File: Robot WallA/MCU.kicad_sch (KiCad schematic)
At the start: 0 parts

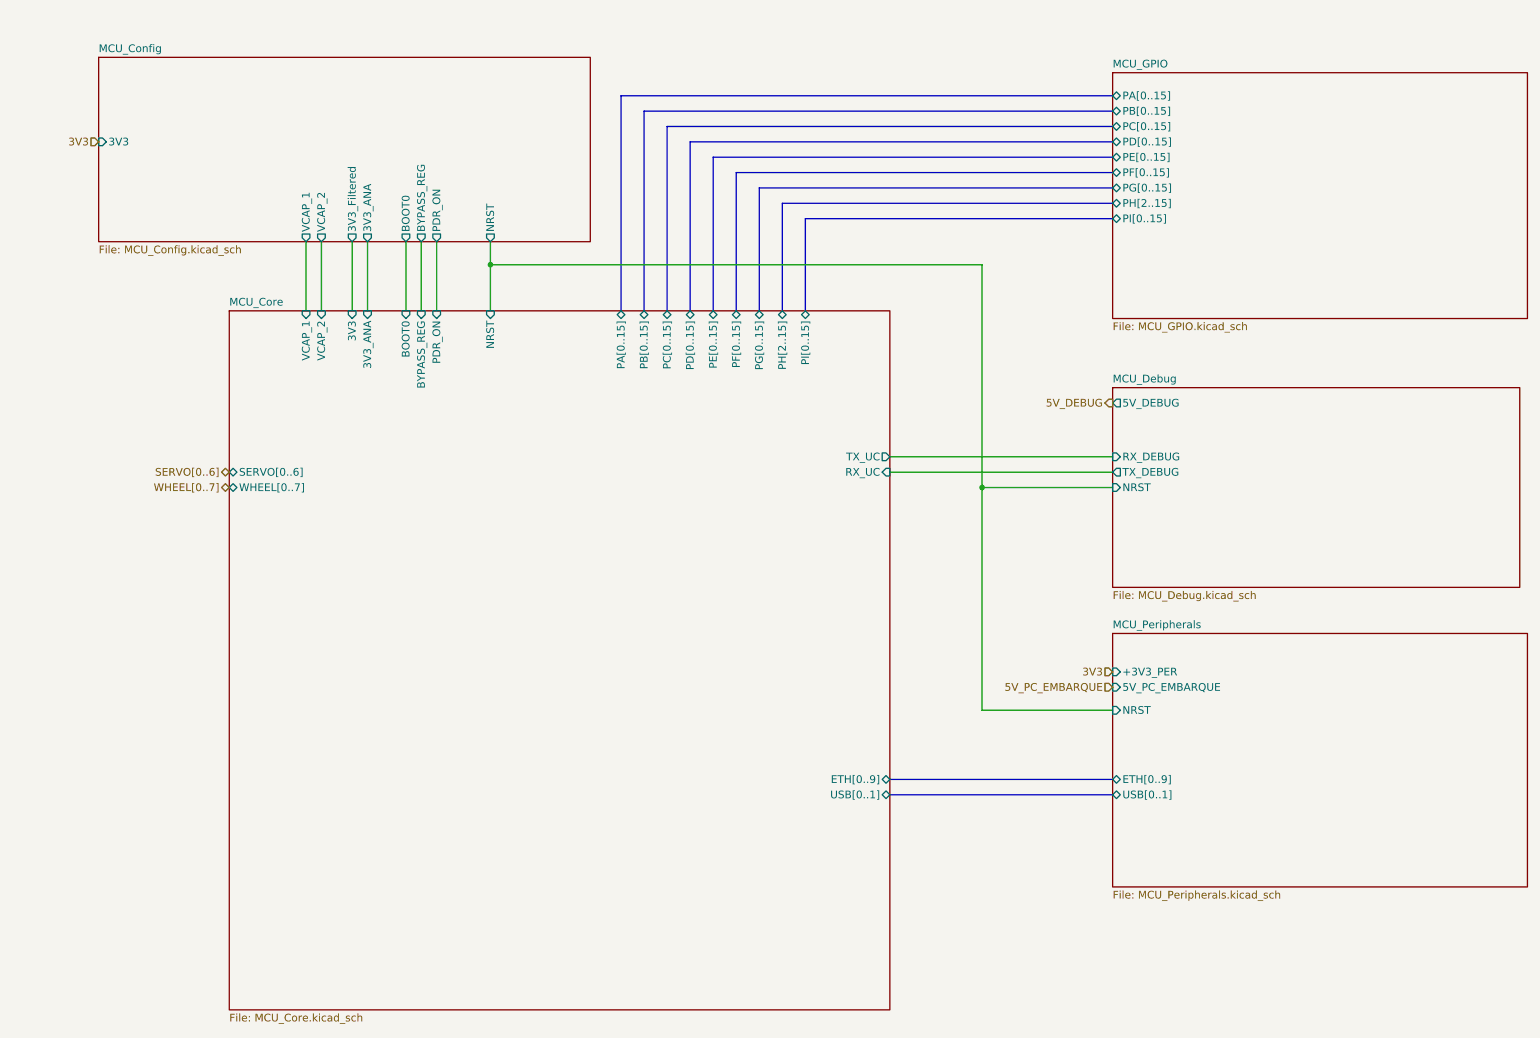
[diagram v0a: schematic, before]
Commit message: Continued to link MCU pins, Added a sheet for servomotors and optional 2 DC motors.
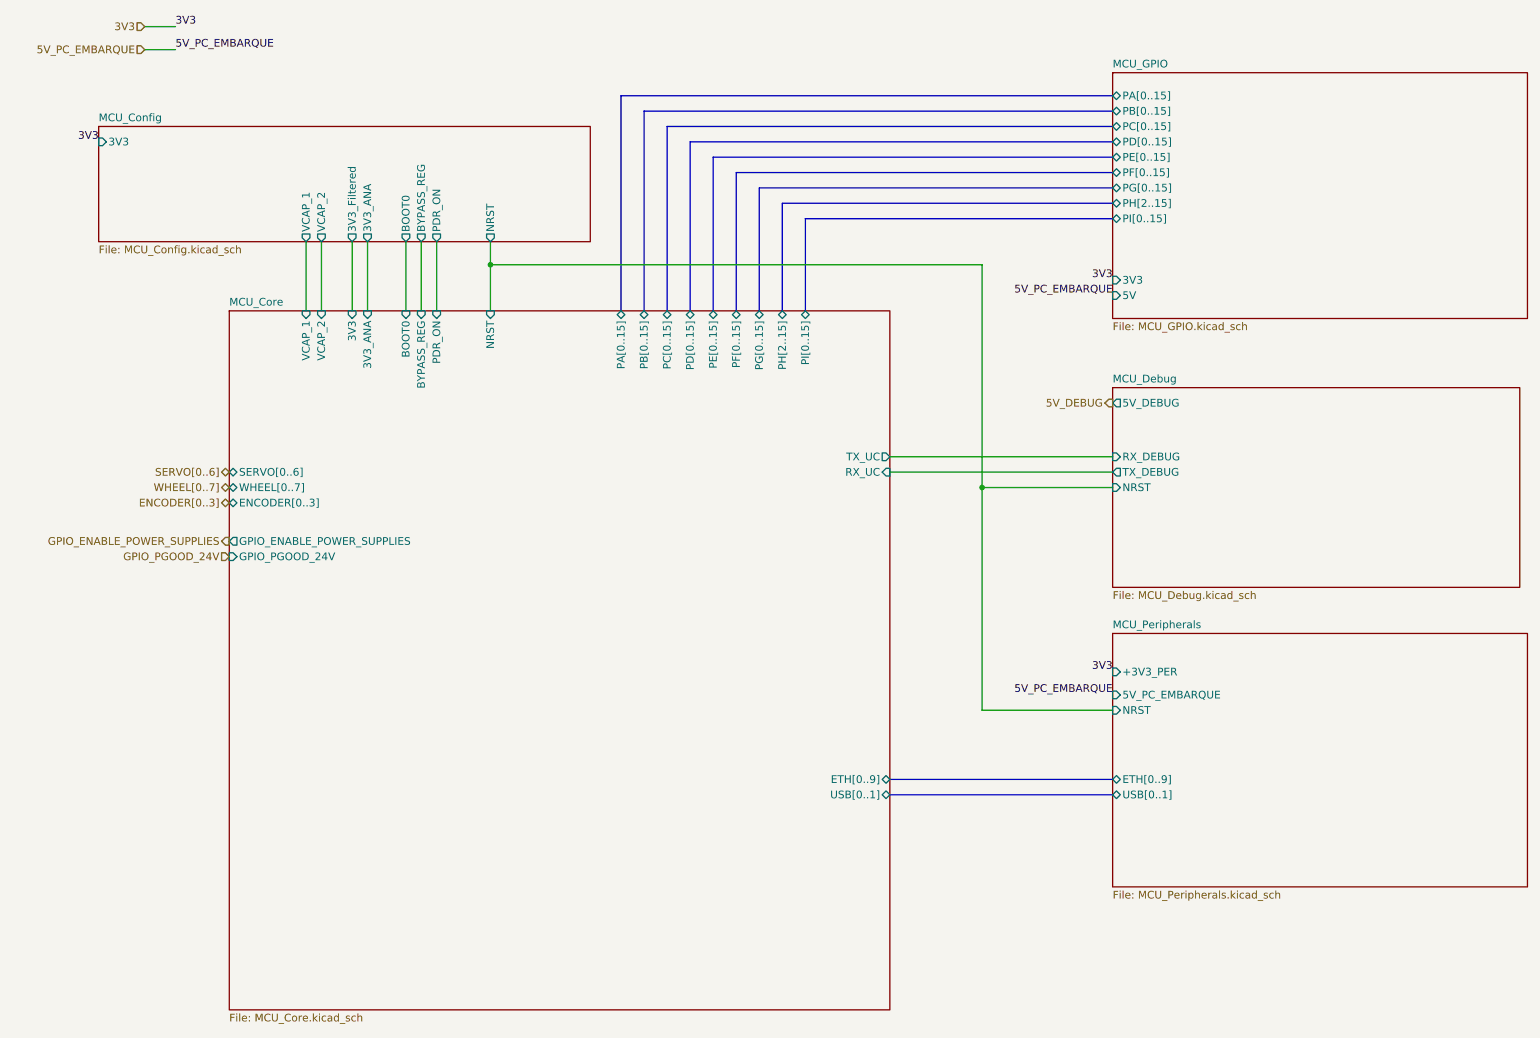
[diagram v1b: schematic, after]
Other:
- sheet MCU_Core ports: added ENCODER[0..3], GPIO_ENABLE_POWER_SUPPLIES, GPIO_PGOOD_24V; removed none
- sheet MCU_GPIO ports: added 3V3, 5V; removed none
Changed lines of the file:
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@@
+		)
+	)
+	(wire
+		(pts
+			(xy 39.37 21.59) (xy 34.29 21.59)
+		)
+		(stroke
+			(width 0)
+			(type default)
+		)
+	)
+	(wire
+		(pts
+			(xy 39.37 17.78) (xy 34.29 17.78)
+		)
+		(stroke
+			(width 0)
+			(type default)
 		)
 	)
@@
 			(width 0)
 			(type default)
+		)
+	)
+	(label "5V_PC_EMBARQUE"
+		(at 194.31 128.27 180)
+		(effects
+			(font
+				(size 1.27 1.27)
+			)
+			(justify right bottom)
+		)
+	)
+	(label "5V_PC_EMBARQUE"
+		(at 39.37 21.59 0)
+		(effects
+			(font
+				(size 1.27 1.27)
+			)
+			(justify left bottom)
+		)
+	)
+	(label "3V3"
+		(at 26.67 36.83 180)
+		(effects
+			(font
+				(size 1.27 1.27)
+			)
+			(justify right bottom)
+		)
+	)
+	(label "3V3"
+		(at 194.31 59.69 180)
+		(effects
+			(font
+				(size 1.27 1.27)
+			)
+			(justify right bottom)
+		)
+	)
+	(label "3V3"
+		(at 39.37 17.78 0)
+		(effects
+			(font
+				(size 1.27 1.27)
+			)
+			(justify left bottom)
+		)
+	)
+	(label "3V3"
+		(at 194.31 124.46 180)
+		(effects
+			(font
+				(size 1.27 1.27)
+			)
+			(justify right bottom)
+		)
+	)
+	(label "5V_PC_EMBARQUE"
+		(at 194.31 62.23 180)
+		(effects
+			(font
+				(size 1.27 1.27)
+			)
+			(justify right bottom)
+		)
+	)
+	(hierarchical_label "GPIO_PGOOD_24V"
+		(shape input)
+		(at 48.26 105.41 180)
+		(effects
+			(font
+				(size 1.27 1.27)
+			)
+			(justify right)
 		)
 	)
@@
 		)
 	)
-	(hierarchical_label "5V_PC_EMBARQUE"
-		(shape input)
-		(at 194.31 127 180)
-		(effects
-			(font
-				(size 1.27 1.27)
-			)
-			(justify right)
-		)
-	)
-	(hierarchical_label "3V3"
-		(shape input)
-		(at 26.67 36.83 180)
-		(effects
-			(font
-				(size 1.27 1.27)
-			)
-			(justify right)
-		)
-	)
 	(hierarchical_label "SERVO[0..6]"
 		(shape bidirectional)
@@
 		)
 	)
+	(hierarchical_label "ENCODER[0..3]"
+		(shape bidirectional)
+		(at 48.26 96.52 180)
+		(effects
+			(font
+				(size 1.27 1.27)
+			)
+			(justify right)
+		)
+	)
+	(hierarchical_label "5V_PC_EMBARQUE"
+		(shape input)
+		(at 34.29 21.59 180)
+		(effects
+			(font
+				(size 1.27 1.27)
+			)
+			(justify right)
+		)
+	)
+	(hierarchical_label "GPIO_ENABLE_POWER_SUPPLIES"
+		(shape output)
+		(at 48.26 102.87 180)
+		(effects
+			(font
+				(size 1.27 1.27)
+			)
+			(justify right)
+		)
+	)
 	(hierarchical_label "3V3"
 		(shape input)
-		(at 194.31 124.46 180)
+		(at 34.29 17.78 180)
 		(effects
 			(font
@@
 		)
 		(instances
-			(project "PCB"
+			(project "Robot WallA"
 				(path "/117fd49e-499d-4b54-b58c-f6b538ecca4a/b9176f6a-4299-4bca-a59b-5ff3df09c616"
 					(page "6")
@@
 		)
 		(pin "5V_PC_EMBARQUE" input
-			(at 194.31 127 180)
+			(at 194.31 128.27 180)
 			(effects
 				(font
@@
 		)
 		(instances
-			(project "PCB"
+			(project "Robot WallA"
 				(path "/117fd49e-499d-4b54-b58c-f6b538ecca4a/b9176f6a-4299-4bca-a59b-5ff3df09c616"
 					(page "8")
@@
 	)
 	(sheet
-		(at 26.67 22.86)
-		(size 81.28 30.48)
+		(at 26.67 34.29)
+		(size 81.28 19.05)
 		(exclude_from_sim no)
 		(in_bom yes)
@@
 		)
 		(property "Sheetname" "MCU_Config"
-			(at 26.67 22.1484 0)
+			(at 26.67 33.5784 0)
 			(effects
 				(font
@@
 		)
 		(instances
-			(project "PCB"
+			(project "Robot WallA"
 				(path "/117fd49e-499d-4b54-b58c-f6b538ecca4a/b9176f6a-4299-4bca-a59b-5ff3df09c616"
 					(page "9")
@@
 			)
 		)
+		(pin "ENCODER[0..3]" bidirectional
+			(at 48.26 96.52 180)
+			(effects
+				(font
+					(size 1.27 1.27)
+				)
+				(justify left)
+			)
+		)
+		(pin "GPIO_ENABLE_POWER_SUPPLIES" output
+			(at 48.26 102.87 180)
+			(effects
+				(font
+					(size 1.27 1.27)
+				)
+				(justify left)
+			)
+		)
+		(pin "GPIO_PGOOD_24V" input
+			(at 48.26 105.41 180)
+			(effects
+				(font
+					(size 1.27 1.27)
+				)
+				(justify left)
+			)
+		)
 		(instances
-			(project "PCB"
+			(project "Robot WallA"
 				(path "/117fd49e-499d-4b54-b58c-f6b538ecca4a/b9176f6a-4299-4bca-a59b-5ff3df09c616"
 					(page "10")
@@
 			)
 		)
+		(pin "3V3" input
+			(at 194.31 59.69 180)
+			(effects
+				(font
+					(size 1.27 1.27)
+				)
+				(justify left)
+			)
+		)
+		(pin "5V" input
+			(at 194.31 62.23 180)
+			(effects
+				(font
+					(size 1.27 1.27)
+				)
+				(justify left)
+			)
+		)
 		(instances
-			(project "PCB"
+			(project "Robot WallA"
 				(path "/117fd49e-499d-4b54-b58c-f6b538ecca4a/b9176f6a-4299-4bca-a59b-5ff3df09c616"
 					(page "7")

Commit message: Defined every footprints
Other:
- sheet MCU_Core ports: added SECONDARY_MOTOR[0..7]; removed none
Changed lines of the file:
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@@
+		)
+	)
+	(hierarchical_label "SECONDARY_MOTOR[0..7]"
+		(shape bidirectional)
+		(at 48.26 91.44 180)
+		(effects
+			(font
+				(size 1.27 1.27)
+			)
+			(justify right)
 		)
 	)
@@
 	(hierarchical_label "WHEEL[0..7]"
 		(shape bidirectional)
-		(at 48.26 93.98 180)
+		(at 48.26 86.36 180)
 		(effects
 			(font
@@
 	(hierarchical_label "SERVO[0..6]"
 		(shape bidirectional)
-		(at 48.26 91.44 180)
+		(at 48.26 83.82 180)
 		(effects
 			(font
@@
 	(hierarchical_label "ENCODER[0..3]"
 		(shape bidirectional)
-		(at 48.26 96.52 180)
+		(at 48.26 88.9 180)
 		(effects
 			(font
@@
 			(project "Robot WallA"
 				(path "/117fd49e-499d-4b54-b58c-f6b538ecca4a/b9176f6a-4299-4bca-a59b-5ff3df09c616"
-					(page "8")
+					(page "5")
 				)
 			)
@@
 			(project "Robot WallA"
 				(path "/117fd49e-499d-4b54-b58c-f6b538ecca4a/b9176f6a-4299-4bca-a59b-5ff3df09c616"
-					(page "9")
+					(page "4")
 				)
 			)
@@
 		)
 		(pin "SERVO[0..6]" bidirectional
-			(at 48.26 91.44 180)
+			(at 48.26 83.82 180)
 			(effects
 				(font
@@
 		)
 		(pin "WHEEL[0..7]" bidirectional
-			(at 48.26 93.98 180)
+			(at 48.26 86.36 180)
 			(effects
 				(font
@@
 		)
 		(pin "ENCODER[0..3]" bidirectional
-			(at 48.26 96.52 180)
+			(at 48.26 88.9 180)
 			(effects
 				(font
@@
 		(pin "GPIO_PGOOD_24V" input
 			(at 48.26 105.41 180)
+			(effects
+				(font
+					(size 1.27 1.27)
+				)
+				(justify left)
+			)
+		)
+		(pin "SECONDARY_MOTOR[0..7]" bidirectional
+			(at 48.26 91.44 180)
 			(effects
 				(font
@@
 			(project "Robot WallA"
 				(path "/117fd49e-499d-4b54-b58c-f6b538ecca4a/b9176f6a-4299-4bca-a59b-5ff3df09c616"
-					(page "10")
-				)
-			)
+					(page "3")
+				)
+			)

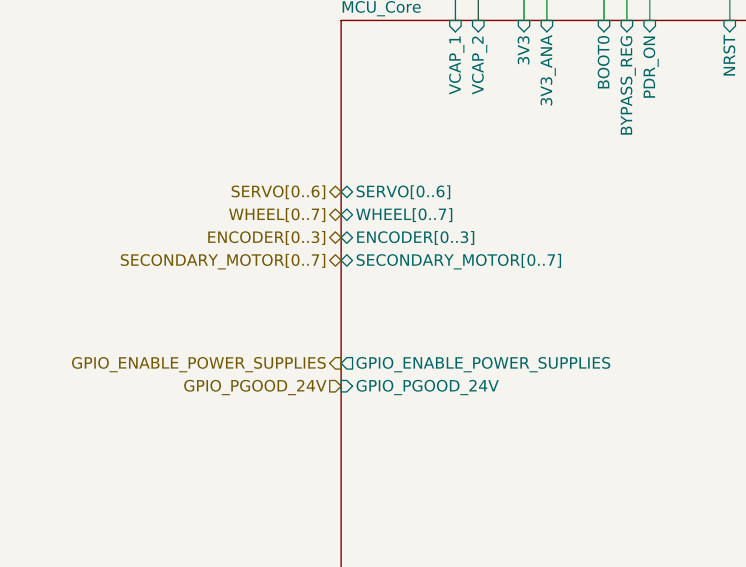
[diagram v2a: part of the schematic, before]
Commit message: Updated USB UART converter, Linked telemeter sensors.
Updated components indicators
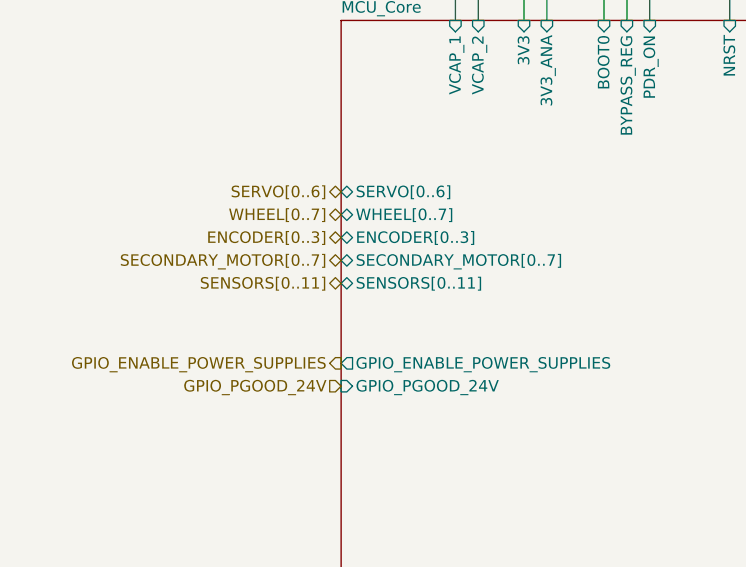
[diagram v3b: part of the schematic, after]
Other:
- sheet MCU_Core ports: added SENSORS[0..11]; removed none
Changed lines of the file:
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@@
+		)
+	)
+	(hierarchical_label "SENSORS[0..11]"
+		(shape bidirectional)
+		(at 48.26 93.98 180)
+		(effects
+			(font
+				(size 1.27 1.27)
+			)
+			(justify right)
 		)
 	)
@@
 			(effects
 				(font
+					(size 1.27 1.27)
+				)
+				(justify left)
+			)
+		)
+		(pin "SENSORS[0..11]" bidirectional
+			(at 48.26 93.98 180)
+			(effects
+				(font

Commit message: Added standard switchs, debug leds and 12V and 5V connectors
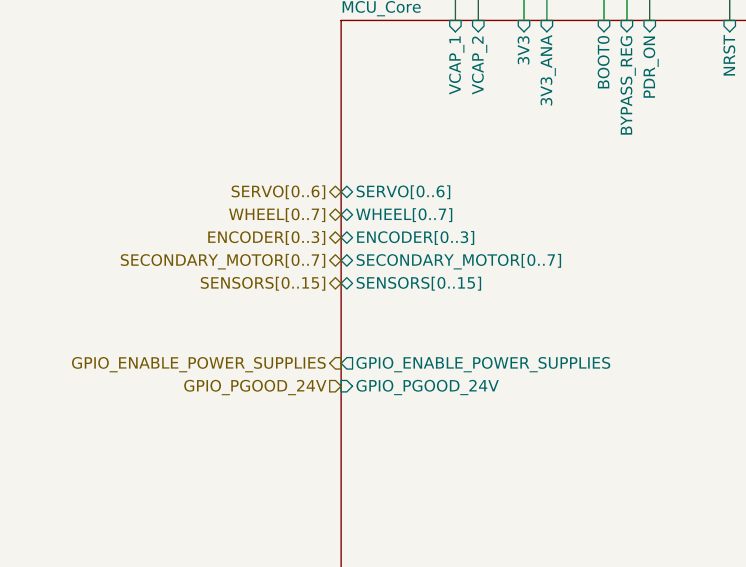
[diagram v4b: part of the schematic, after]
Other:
- sheet MCU_Core ports: added SENSORS[0..15]; removed SENSORS[0..11]
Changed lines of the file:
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@@
 		)
 	)
-	(hierarchical_label "SENSORS[0..11]"
+	(hierarchical_label "SENSORS[0..15]"
 		(shape bidirectional)
 		(at 48.26 93.98 180)
@@
 			)
 		)
-		(pin "SENSORS[0..11]" bidirectional
+		(pin "SENSORS[0..15]" bidirectional
 			(at 48.26 93.98 180)
 			(effects

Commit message: Correct a lot of error in DRC
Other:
- sheet MCU_Peripherals ports: added 3V3; removed +3V3_PER
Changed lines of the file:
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@@
 			)
 		)
-		(pin "+3V3_PER" input
+		(pin "3V3" input
 			(at 194.31 124.46 180)
 			(effects

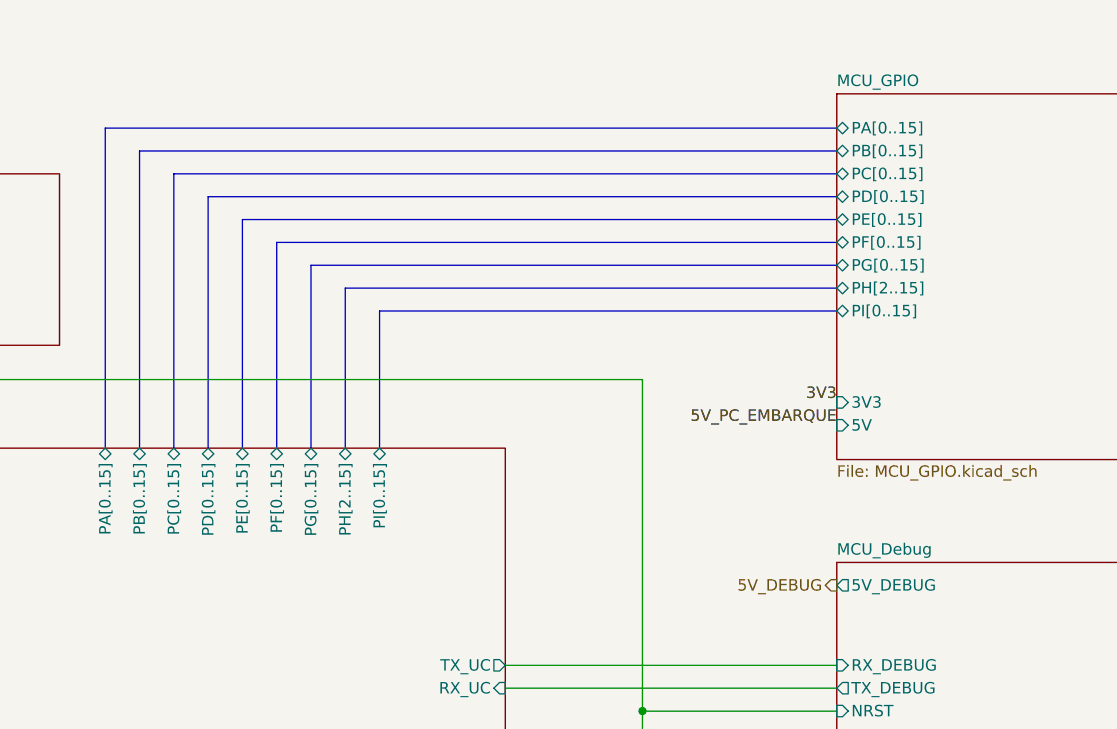
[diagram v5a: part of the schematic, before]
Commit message: Corrected all DRC erros, added info on PCB
modified distance meter connectors to be horizontal
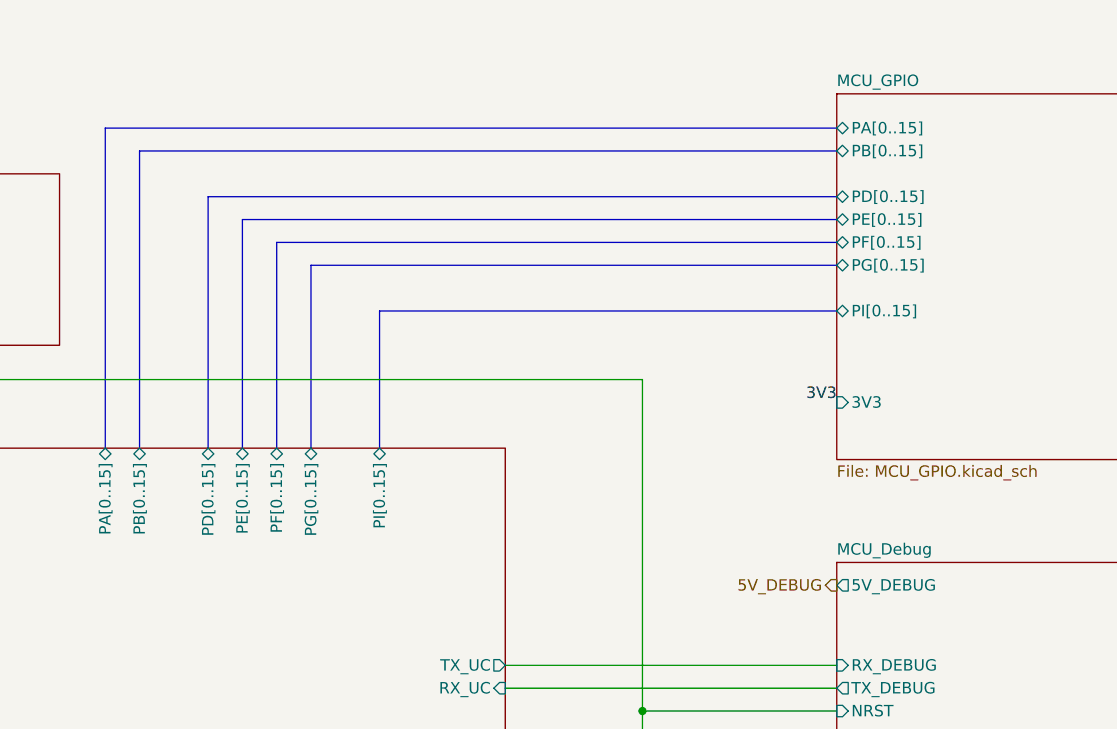
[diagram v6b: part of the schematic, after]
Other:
- sheet MCU_Core ports: added none; removed PC[0..15], PH[2..15]
- sheet MCU_GPIO ports: added none; removed 5V, PC[0..15], PH[2..15]
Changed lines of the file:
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@@
-	(bus
-		(pts
-			(xy 139.7 46.99) (xy 194.31 46.99)
-		)
-		(stroke
-			(width 0)
-			(type default)
-		)
-	)
 	(bus
 		(pts
@@
 	(bus
 		(pts
-			(xy 194.31 34.29) (xy 120.65 34.29)
-		)
-		(stroke
-			(width 0)
-			(type default)
-		)
-	)
-	(bus
-		(pts
 			(xy 132.08 41.91) (xy 194.31 41.91)
 		)
@@
 	(bus
 		(pts
-			(xy 139.7 64.77) (xy 139.7 46.99)
-		)
-		(stroke
-			(width 0)
-			(type default)
-		)
-	)
-	(bus
-		(pts
 			(xy 194.31 49.53) (xy 143.51 49.53)
 		)
@@
 		(pts
 			(xy 157.48 142.24) (xy 194.31 142.24)
-		)
-		(stroke
-			(width 0)
-			(type default)
-		)
-	)
-	(bus
-		(pts
-			(xy 120.65 34.29) (xy 120.65 64.77)
 		)
 		(stroke
@@
 	(label "3V3"
 		(at 194.31 124.46 180)
-		(effects
-			(font
-				(size 1.27 1.27)
-			)
-			(justify right bottom)
-		)
-	)
-	(label "5V_PC_EMBARQUE"
-		(at 194.31 62.23 180)
 		(effects
 			(font
@@
 			)
 		)
-		(pin "PC[0..15]" bidirectional
-			(at 120.65 64.77 90)
-			(effects
-				(font
-					(size 1.27 1.27)
-				)
-				(justify right)
-			)
-		)
 		(pin "PD[0..15]" bidirectional
 			(at 124.46 64.77 90)
@@
 		(pin "PG[0..15]" bidirectional
 			(at 135.89 64.77 90)
-			(effects
-				(font
-					(size 1.27 1.27)
-				)
-				(justify right)
-			)
-		)
-		(pin "PH[2..15]" bidirectional
-			(at 139.7 64.77 90)
 			(effects
 				(font
@@
 			)
 		)
-		(pin "PC[0..15]" bidirectional
-			(at 194.31 34.29 180)
-			(effects
-				(font
-					(size 1.27 1.27)
-				)
-				(justify left)
-			)
-		)
 		(pin "PD[0..15]" bidirectional
 			(at 194.31 36.83 180)
@@
 			)
 		)
-		(pin "PH[2..15]" bidirectional
-			(at 194.31 46.99 180)
-			(effects
-				(font
-					(size 1.27 1.27)
-				)
-				(justify left)
-			)
-		)
 		(pin "PI[0..15]" bidirectional
 			(at 194.31 49.53 180)
@@
 			(effects
 				(font
-					(size 1.27 1.27)
-				)
-				(justify left)
-			)
-		)
-		(pin "5V" input
-			(at 194.31 62.23 180)
-			(effects
-				(font

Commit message: Updated fab files.
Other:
- company: (none) -> Socotec Monitoring
- title: (none) -> Robot Wall-A
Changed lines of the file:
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@@
 	(generator_version "9.0")
 	(paper "A4")
+	(title_block
+		(title "Robot Wall-A")
+		(date "2025-09-20")
+		(rev "v1.0")
+		(company "Socotec Monitoring")
+		(comment 1 "GDU")
+		(comment 2 "THO")
+	)
 	(junction
 		(at 172.72 93.98)
